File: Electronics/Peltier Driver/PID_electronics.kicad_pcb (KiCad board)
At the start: 2 copper layers, 73.2 x 43.8 mm, 29 parts, among them J1 Conn_01x05, J2 Conn_01x03, Q3 2N7000, U1 LF412

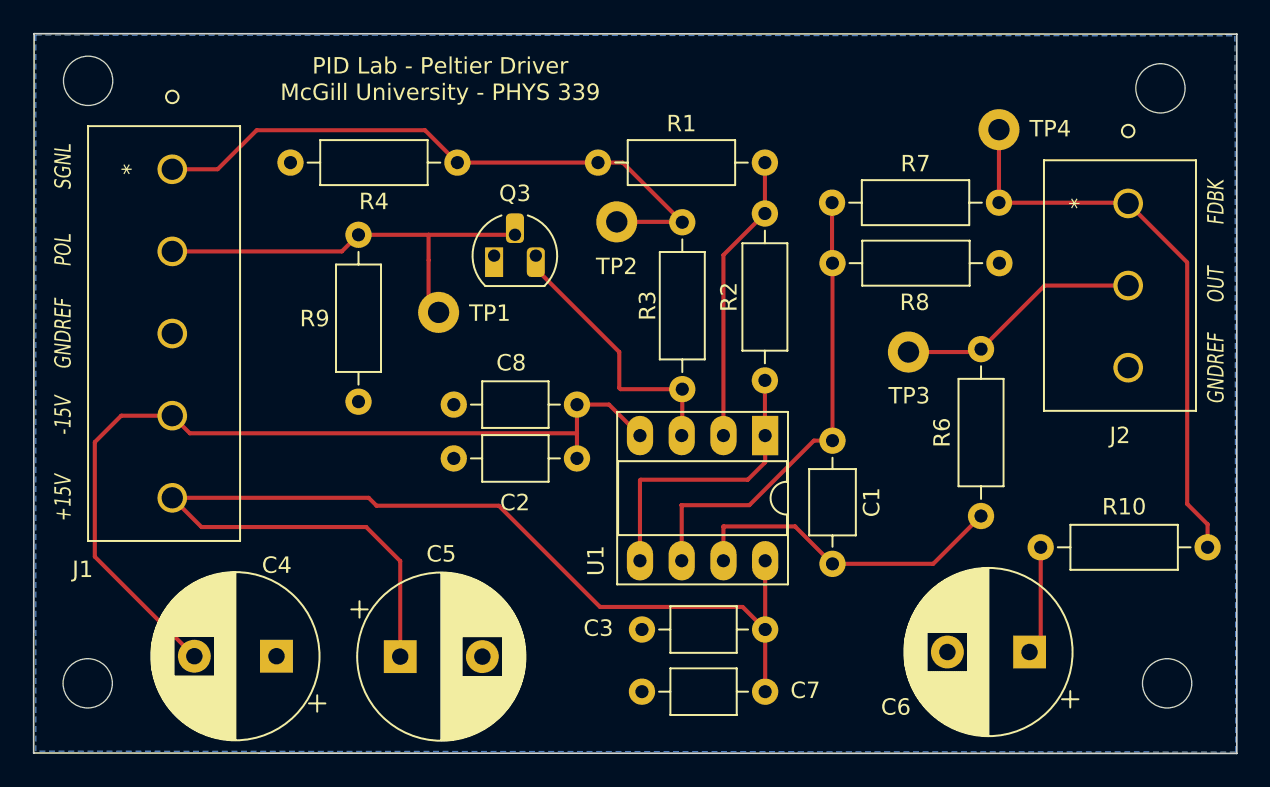
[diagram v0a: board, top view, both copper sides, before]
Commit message: 2N7000 footprint change, gerbers generated
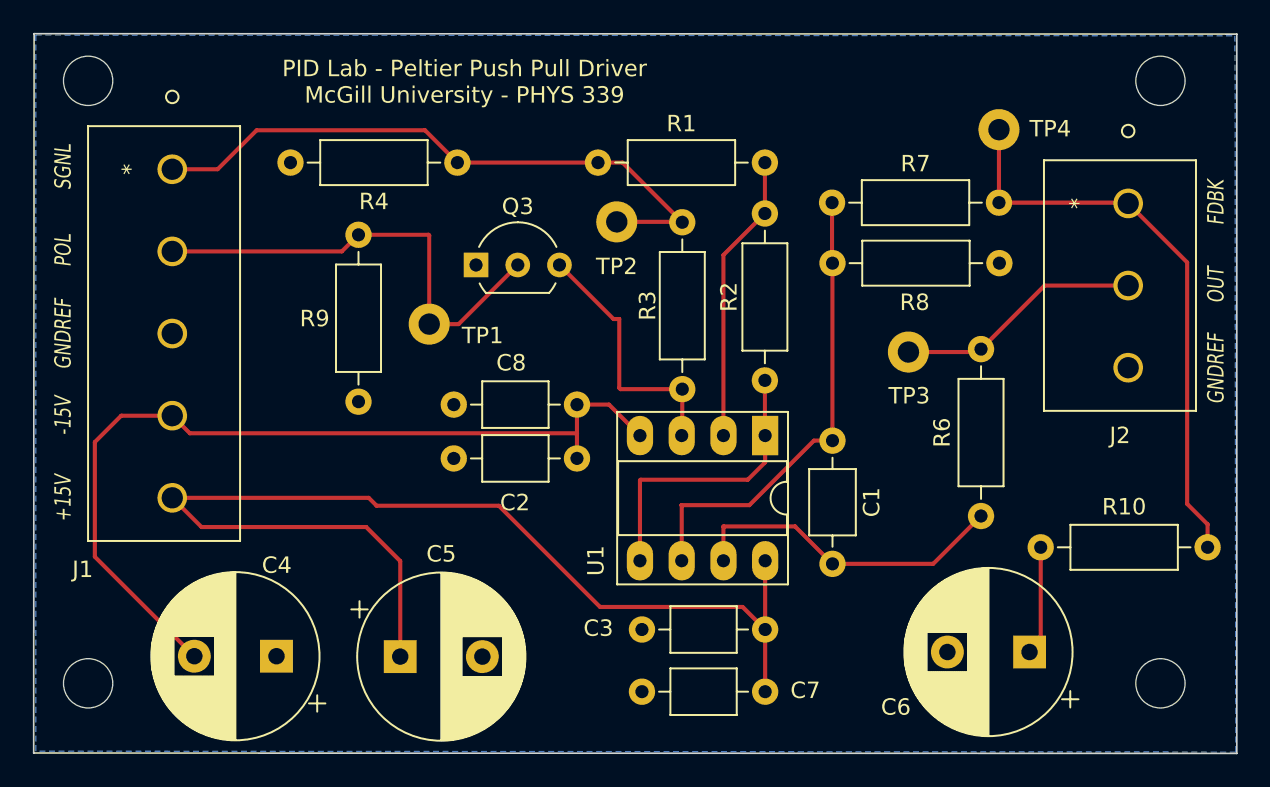
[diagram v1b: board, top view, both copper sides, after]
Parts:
- Q3: footprint Package_TO_SOT_THT:TO-92_HandSolder -> Package_TO_SOT_THT:TO-92L_Inline_Wide
- moved Q3 1.24 mm to (113.2, 83.6)
- moved REF** 0.91 mm to (110.3, 94.8)
- moved REF** 0.46 mm to (154.9, 77.5)
- moved REF** 0.41 mm to (154.9, 114.1)
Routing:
- net Net-(Q3-Pad2): track 26.3 -> 29.2 mm
- net Net-(Q3-Pad3): track 16.9 -> 15.9 mm
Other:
- board text added: "PID Lab - Peltier Push Pull Driver McGill University - PHYS 339"
- board text removed: "PID Lab - Peltier Driver McGill University - PHYS 339"
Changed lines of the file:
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@@
       (net 4 "GNDREF") (pinfunction "Pin_3") (pintype "passive"))
   )
-  (footprint "Package_TO_SOT_THT:TO-92_HandSolder" (layer "F.Cu")
-    (at 114.3 83.0326)
-    (descr "TO-92 leads molded, narrow, drill 0.75mm, handsoldering variant with enlarged pads (see NXP sot054_po.pdf)")
-    (tags "to-92 sc-43 sc-43a sot54 PA33 transistor")
-    (property "Sheetfile" "PID_electronics.kicad_sch")
-    (property "Sheetname" "")
-    (attr through_hole)
-    (fp_text reference "Q3" (at 1.27 -3.7846) (layer "F.SilkS")
-      (effects (font (size 1 1) (thickness 0.15)))
-    )
-    (fp_text value "2N7000" (at 1.27 2.79) (layer "F.Fab")
-      (effects (font (size 1 1) (thickness 0.15)))
-    )
-    (fp_text user "${REFERENCE}" (at 1.27 0) (layer "F.Fab")
-      (effects (font (size 1 1) (thickness 0.15)))
-    )
-    (fp_line (start -0.53 1.85) (end 3.07 1.85) (layer "F.SilkS") (width 0.12))
-    (fp_arc (start 2.05 -2.45) (mid 3.769931 -0.601036) (end 3.078445 1.827684) (layer "F.SilkS") (width 0.12))
-    (fp_arc (start -0.541875 1.841741) (mid -1.247231 -0.581764) (end 0.45 -2.45) (layer "F.SilkS") (width 0.12))
-    (fp_line (start -1.46 -3.05) (end -1.46 2.01) (layer "F.CrtYd") (width 0.05))
-    (fp_line (start -1.46 -3.05) (end 4 -3.05) (layer "F.CrtYd") (width 0.05))
-    (fp_line (start 4 2.01) (end -1.46 2.01) (layer "F.CrtYd") (width 0.05))
-    (fp_line (start 4 2.01) (end 4 -3.05) (layer "F.CrtYd") (width 0.05))
-    (fp_line (start -0.5 1.75) (end 3 1.75) (layer "F.Fab") (width 0.1))
-    (fp_arc (start -0.483625 1.753625) (mid -1.021221 -0.949055) (end 1.27 -2.48) (layer "F.Fab") (width 0.1))
-    (fp_arc (start 1.27 -2.48) (mid 3.561221 -0.949055) (end 3.023625 1.753625) (layer "F.Fab") (width 0.1))
-    (pad "1" thru_hole rect locked (at 0 0) (size 1.1 1.8) (drill 0.75 (offset 0 0.4)) (layers *.Cu *.Mask)
+  (footprint "Package_TO_SOT_THT:TO-92L_Inline_Wide" (layer "F.Cu")
+    (at 113.2 83.6)
+    (descr "TO-92L leads in-line (large body variant of TO-92), also known as TO-226, wide, drill 0.75mm (see https://www.diodes.com/assets/Package-Files/TO92L.pdf and http://www.ti.com/lit/an/snoa059/snoa059.pdf)")
+    (tags "TO-92L Inline Wide transistor")
+    (property "Sheetfile" "PID_electronics.kicad_sch")
+    (property "Sheetname" "")
+    (attr through_hole)
+    (fp_text reference "Q3" (at 2.54 -3.56) (layer "F.SilkS")
+      (effects (font (size 1 1) (thickness 0.15)))
+    )
+    (fp_text value "2N7000" (at 2.54 2.79) (layer "F.Fab")
+      (effects (font (size 1 1) (thickness 0.15)))
+    )
+    (fp_text user "${REFERENCE}" (at 2.54 0) (layer "F.Fab")
+      (effects (font (size 1 1) (thickness 0.15)))
+    )
+    (fp_line (start 0.6 1.7) (end 4.45 1.7) (layer "F.SilkS") (width 0.12))
+    (fp_arc (start 2.54 -2.6) (mid 3.936979 -2.192818) (end 4.8964 -1.098807) (layer "F.SilkS") (width 0.12))
+    (fp_arc (start 0.6 1.7) (mid 0.389183 1.423933) (end 0.217369 1.122045) (layer "F.SilkS") (width 0.12))
+    (fp_arc (start 4.842383 1.112264) (mid 4.666594 1.419753) (end 4.45 1.7) (layer "F.SilkS") (width 0.12))
+    (fp_arc (start 0.1836 -1.098807) (mid 1.143021 -2.192817) (end 2.54 -2.6) (layer "F.SilkS") (width 0.12))
+    (fp_line (start 6.1 1.85) (end -1 1.85) (layer "F.CrtYd") (width 0.05))
+    (fp_line (start -1 -2.75) (end 6.1 -2.75) (layer "F.CrtYd") (width 0.05))
+    (fp_line (start 6.1 1.85) (end 6.1 -2.75) (layer "F.CrtYd") (width 0.05))
+    (fp_line (start -1 -2.75) (end -1 1.85) (layer "F.CrtYd") (width 0.05))
+    (fp_line (start 0.65 1.6) (end 4.4 1.6) (layer "F.Fab") (width 0.1))
+    (fp_arc (start 2.54 -2.48) (mid 4.787211 -1.049019) (end 4.441103 1.592547) (layer "F.Fab") (width 0.1))
+    (fp_arc (start 0.647182 1.602385) (mid 0.290076 -1.043188) (end 2.54 -2.48) (layer "F.Fab") (width 0.1))
+    (pad "1" thru_hole rect locked (at 0 0) (size 1.5 1.5) (drill 0.8) (layers *.Cu *.Mask)
       (net 4 "GNDREF") (pinfunction "S") (pintype "passive"))
-    (pad "2" thru_hole roundrect locked (at 1.27 -1.27) (size 1.1 1.8) (drill 0.75 (offset 0 -0.4)) (layers *.Cu *.Mask) (roundrect_rratio 0.25)
+    (pad "2" thru_hole circle locked (at 2.54 0) (size 1.5 1.5) (drill 0.8) (layers *.Cu *.Mask)
       (net 12 "Net-(Q3-Pad2)") (pinfunction "G") (pintype "input"))
-    (pad "3" thru_hole roundrect locked (at 2.54 0) (size 1.1 1.8) (drill 0.75 (offset 0 0.4)) (layers *.Cu *.Mask) (roundrect_rratio 0.25)
+    (pad "3" thru_hole circle locked (at 5.08 0) (size 1.5 1.5) (drill 0.8) (layers *.Cu *.Mask)
       (net 5 "Net-(Q3-Pad3)") (pinfunction "D") (pintype "passive"))
-    (model "${KICAD6_3DMODEL_DIR}/Package_TO_SOT_THT.3dshapes/TO-92.wrl"
+    (model "${KICAD6_3DMODEL_DIR}/Package_TO_SOT_THT.3dshapes/TO-92L_Inline_Wide.wrl"
       (offset (xyz 0 0 0))
       (scale (xyz 1 1 1))
@@
   )
   (footprint "KiCAD_footprints:mounting hole" (layer "F.Cu")
-    (at 89.5604 114.1476)
+    (at 89.5858 114.1476)
     (attr through_hole)
     (fp_text reference "REF**" (at 0 -0.5 unlocked) (layer "F.SilkS") hide
@@
   )
   (footprint "KiCAD_footprints:Test_point" (layer "F.Cu")
-    (at 110.9218 94.107)
+    (at 110.35 94.82)
     (attr through_hole)
     (fp_text reference "REF**" (at 0 -0.5 unlocked) (layer "F.SilkS") hide
       (effects (font (size 1 1) (thickness 0.15)))
     )
-    (fp_text value "TP1" (at 3.1242 -7.5692 unlocked) (layer "F.SilkS")
+    (fp_text value "TP1" (at 3.25 -6.92 unlocked) (layer "F.SilkS")
       (effects (font (size 1 1) (thickness 0.15)))
     )
@@
   )
   (footprint "KiCAD_footprints:mounting hole" (layer "F.Cu")
-    (at 155.2702 114.1476)
+    (at 154.8638 114.1476)
     (attr through_hole)
     (fp_text reference "REF**" (at 0 -0.5 unlocked) (layer "F.SilkS") hide
@@
   )
   (footprint "KiCAD_footprints:mounting hole" (layer "F.Cu")
-    (at 154.8638 77.9272)
+    (at 154.8638 77.47)
     (attr through_hole)
     (fp_text reference "REF**" (at 0 -0.5 unlocked) (layer "F.SilkS") hide
@@
     (effects (font (size 1 0.75) (thickness 0.1875) italic))
   )
-  (gr_text "PID Lab - Peltier Driver\nMcGill University - PHYS 339" (at 111.0234 72.2884) (layer "F.SilkS")
+  (gr_text "PID Lab - Peltier Push Pull Driver\nMcGill University - PHYS 339" (at 112.5 72.45) (layer "F.SilkS")
     (effects (font (size 1 1) (thickness 0.15)))
   )
@@
   (segment (start 129.4292 104.4194) (end 130.8008 105.791) (width 0.25) (layer "F.Cu") (net 3))
   (segment (start 96.4871 99.553) (end 106.5126 99.553) (width 0.25) (layer "F.Cu") (net 3))
+  (segment (start 121.9962 91.1606) (end 125.7554 91.1606) (width 0.25) (layer "F.Cu") (net 5))
+  (segment (start 121.57 86.89) (end 121.92 86.89) (width 0.25) (layer "F.Cu") (net 5))
+  (segment (start 125.7554 91.1606) (end 125.7554 93.9496) (width 0.25) (layer "F.Cu") (net 5))
+  (segment (start 125.7554 93.9496) (end 125.72 93.985) (width 0.25) (layer "F.Cu") (net 5))
   (segment (start 121.92 91.0844) (end 121.9962 91.1606) (width 0.25) (layer "F.Cu") (net 5))
-  (segment (start 125.7554 91.1606) (end 125.7554 93.9496) (width 0.25) (layer "F.Cu") (net 5))
-  (segment (start 121.9962 91.1606) (end 125.7554 91.1606) (width 0.25) (layer "F.Cu") (net 5))
-  (segment (start 125.7554 93.9496) (end 125.72 93.985) (width 0.25) (layer "F.Cu") (net 5))
-  (segment (start 116.84 83.0326) (end 116.84 83.82) (width 0.25) (layer "F.Cu") (net 5))
-  (segment (start 121.92 88.9) (end 121.92 91.0844) (width 0.25) (layer "F.Cu") (net 5))
-  (segment (start 116.84 83.82) (end 121.92 88.9) (width 0.25) (layer "F.Cu") (net 5))
+  (segment (start 118.28 83.6) (end 121.57 86.89) (width 0.25) (layer "F.Cu") (net 5))
+  (segment (start 121.92 86.89) (end 121.92 91.0844) (width 0.25) (layer "F.Cu") (net 5))
   (segment (start 130.7846 80.4672) (end 128.26 82.9918) (width 0.25) (layer "F.Cu") (net 6))
   (segment (start 128.26 82.9918) (end 128.26 93.985) (width 0.25) (layer "F.Cu") (net 6))
@@
   (segment (start 147.574 100.7872) (end 147.574 106.482277) (width 0.25) (layer "F.Cu") (net 11))
   (segment (start 147.574 106.482277) (end 146.893677 107.1626) (width 0.25) (layer "F.Cu") (net 11))
+  (segment (start 110.35 81.8004) (end 110.35 87.2) (width 0.25) (layer "F.Cu") (net 12))
+  (segment (start 112.14 87.2) (end 115.74 83.6) (width 0.25) (layer "F.Cu") (net 12))
   (segment (start 106.045 81.7626) (end 110.3122 81.7626) (width 0.25) (layer "F.Cu") (net 12))
-  (segment (start 110.3122 81.7626) (end 110.3122 83.312) (width 0.25) (layer "F.Cu") (net 12))
-  (segment (start 110.3122 85.8774) (end 110.9218 86.487) (width 0.25) (layer "F.Cu") (net 12))
+  (segment (start 109.9904 87.0404) (end 110.6 87.65) (width 0.25) (layer "F.Cu") (net 12))
   (segment (start 106.045 81.7626) (end 105.033101 82.774499) (width 0.25) (layer "F.Cu") (net 12))
   (segment (start 105.033101 82.774499) (end 94.7086 82.774499) (width 0.25) (layer "F.Cu") (net 12))
-  (segment (start 110.3122 83.312) (end 110.3122 85.8774) (width 0.25) (layer "F.Cu") (net 12))
-  (segment (start 110.3122 81.7626) (end 115.57 81.7626) (width 0.25) (layer "F.Cu") (net 12))
+  (segment (start 110.35 87.2) (end 112.14 87.2) (width 0.25) (layer "F.Cu") (net 12))
+  (segment (start 110.3122 81.7626) (end 110.35 81.8004) (width 0.25) (layer "F.Cu") (net 12))
   (segment (start 99.8474 75.3976) (end 110.094 75.3976) (width 0.25) (layer "F.Cu") (net 13))
   (segment (start 121.7676 80.9752) (end 125.73 80.9752) (width 0.25) (layer "F.Cu") (net 13))

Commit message: minor layout change
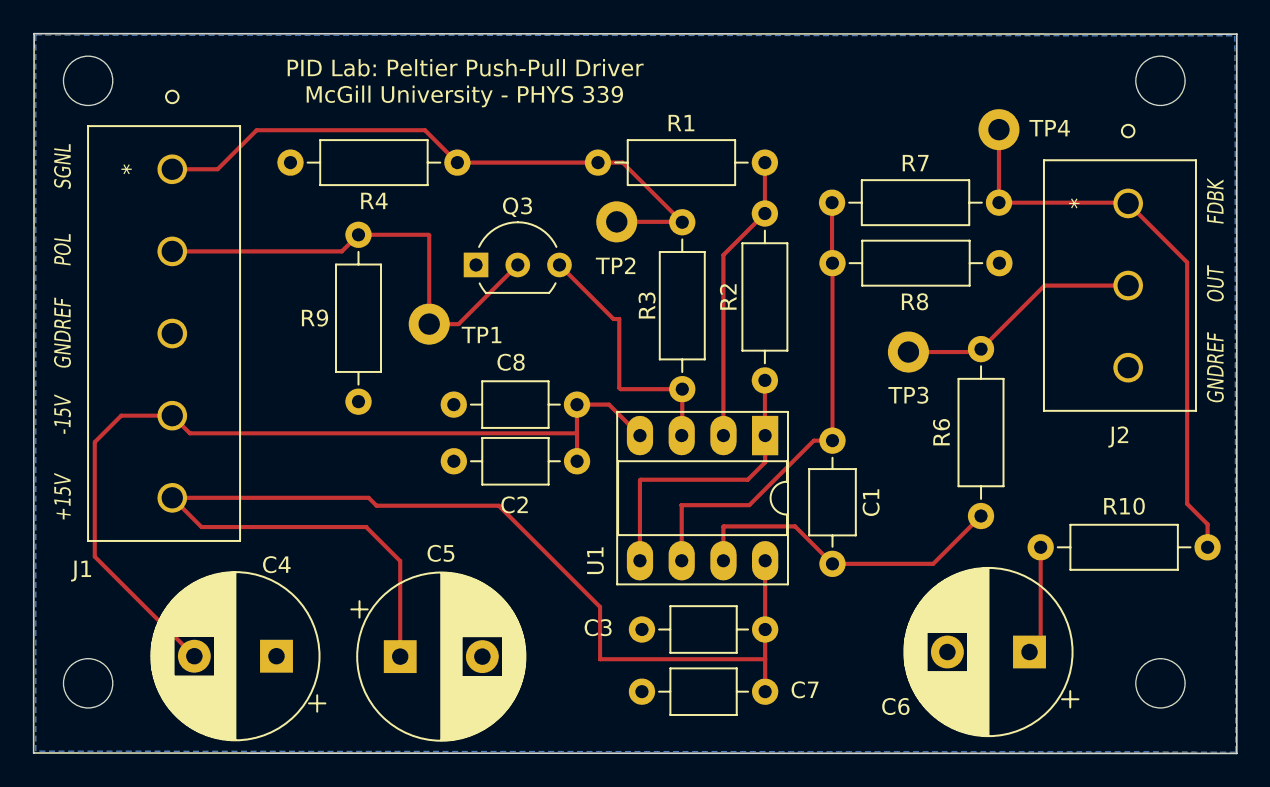
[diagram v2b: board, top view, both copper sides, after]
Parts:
- moved C2 0.17 mm to (111.8, 95.5)
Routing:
- net +15V: track 68.7 -> 71.3 mm
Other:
- board text added: "PID Lab: Peltier Push-Pull Driver McGill University - PHYS 339"
- board text removed: "PID Lab - Peltier Push Pull Driver McGill University - PHYS 339"
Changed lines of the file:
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@@
   )
   (footprint "Capacitor_THT:C_Axial_L3.8mm_D2.6mm_P7.50mm_Horizontal" (layer "F.Cu")
-    (at 111.8454 95.377)
+    (at 111.85 95.55)
     (descr "C, Axial series, Axial, Horizontal, pin pitch=7.5mm, , length*diameter=3.8*2.6mm^2, http://www.vishay.com/docs/45231/arseries.pdf")
     (tags "C Axial series Axial Horizontal pin pitch 7.5mm  length 3.8mm diameter 2.6mm")
@@
     (effects (font (size 1 0.75) (thickness 0.1875) italic))
   )
-  (gr_text "PID Lab - Peltier Push Pull Driver\nMcGill University - PHYS 339" (at 112.5 72.45) (layer "F.SilkS")
+  (gr_text "PID Lab: Peltier Push-Pull Driver\nMcGill University - PHYS 339" (at 112.5 72.45) (layer "F.SilkS")
     (effects (font (size 1 1) (thickness 0.15)))
   )
@@
   (segment (start 141.03 101.794) (end 143.9418 98.8822) (width 0.25) (layer "F.Cu") (net 1))
   (segment (start 134.8994 101.794) (end 141.03 101.794) (width 0.25) (layer "F.Cu") (net 1))
+  (segment (start 119.35 93.8114) (end 119.35 95.55) (width 0.25) (layer "F.Cu") (net 2))
   (segment (start 95.7813 93.8472) (end 119.305 93.8472) (width 0.25) (layer "F.Cu") (net 2))
+  (segment (start 119.3454 93.8068) (end 119.3454 92.1004) (width 0.25) (layer "F.Cu") (net 2))
   (segment (start 121.2954 92.1004) (end 123.18 93.985) (width 0.25) (layer "F.Cu") (net 2))
   (segment (start 119.3454 92.1004) (end 121.2954 92.1004) (width 0.25) (layer "F.Cu") (net 2))
-  (segment (start 119.305 93.8472) (end 119.3454 93.8876) (width 0.25) (layer "F.Cu") (net 2))
-  (segment (start 119.3454 93.8876) (end 119.3454 95.377) (width 0.25) (layer "F.Cu") (net 2))
   (segment (start 89.9922 101.356646) (end 96.052154 107.4166) (width 0.25) (layer "F.Cu") (net 2))
-  (segment (start 119.3454 92.1004) (end 119.3454 93.8876) (width 0.25) (layer "F.Cu") (net 2))
   (segment (start 89.9922 94.3864) (end 89.9922 101.356646) (width 0.25) (layer "F.Cu") (net 2))
   (segment (start 94.7086 92.7745) (end 95.7813 93.8472) (width 0.25) (layer "F.Cu") (net 2))
+  (segment (start 119.3454 93.8068) (end 119.35 93.8114) (width 0.25) (layer "F.Cu") (net 2))
   (segment (start 91.6041 92.7745) (end 89.9922 94.3864) (width 0.25) (layer "F.Cu") (net 2))
+  (segment (start 119.305 93.8472) (end 119.3454 93.8068) (width 0.25) (layer "F.Cu") (net 2))
   (segment (start 94.7086 92.7745) (end 91.6041 92.7745) (width 0.25) (layer "F.Cu") (net 2))
   (segment (start 107.1471 98.2571) (end 114.5893 98.2571) (width 0.25) (layer "F.Cu") (net 3))
-  (segment (start 120.7516 104.4194) (end 129.4292 104.4194) (width 0.25) (layer "F.Cu") (net 3))
   (segment (start 94.7086 97.7745) (end 106.6645 97.7745) (width 0.25) (layer "F.Cu") (net 3))
+  (segment (start 120.75 107.6) (end 130.8 107.6) (width 0.25) (layer "F.Cu") (net 3))
   (segment (start 106.6645 97.7745) (end 107.1471 98.2571) (width 0.25) (layer "F.Cu") (net 3))
   (segment (start 108.585 101.6254) (end 108.585 107.442) (width 0.25) (layer "F.Cu") (net 3))
   (segment (start 106.5126 99.553) (end 108.585 101.6254) (width 0.25) (layer "F.Cu") (net 3))
-  (segment (start 130.8008 105.791) (end 130.8008 109.5756) (width 0.25) (layer "F.Cu") (net 3))
   (segment (start 130.8 101.605) (end 130.8 105.7902) (width 0.25) (layer "F.Cu") (net 3))
   (segment (start 130.8 105.7902) (end 130.8008 105.791) (width 0.25) (layer "F.Cu") (net 3))
+  (segment (start 120.7516 107.5984) (end 120.75 107.6) (width 0.25) (layer "F.Cu") (net 3))
   (segment (start 114.5893 98.2571) (end 120.7516 104.4194) (width 0.25) (layer "F.Cu") (net 3))
   (segment (start 94.7086 97.7745) (end 96.4871 99.553) (width 0.25) (layer "F.Cu") (net 3))
-  (segment (start 129.4292 104.4194) (end 130.8008 105.791) (width 0.25) (layer "F.Cu") (net 3))
+  (segment (start 120.7516 104.4194) (end 120.7516 107.5984) (width 0.25) (layer "F.Cu") (net 3))
+  (segment (start 130.8008 107.5992) (end 130.8008 109.5756) (width 0.25) (layer "F.Cu") (net 3))
+  (segment (start 130.8 107.6) (end 130.8008 107.5992) (width 0.25) (layer "F.Cu") (net 3))
   (segment (start 96.4871 99.553) (end 106.5126 99.553) (width 0.25) (layer "F.Cu") (net 3))
+  (segment (start 130.8008 105.791) (end 130.8008 107.5992) (width 0.25) (layer "F.Cu") (net 3))
   (segment (start 121.9962 91.1606) (end 125.7554 91.1606) (width 0.25) (layer "F.Cu") (net 5))
   (segment (start 121.57 86.89) (end 121.92 86.89) (width 0.25) (layer "F.Cu") (net 5))
